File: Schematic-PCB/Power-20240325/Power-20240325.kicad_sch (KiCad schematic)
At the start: 10 parts, among them J1 Conn_01x02_Pin, Q1 NMOS, Q2 PMOS, U1 PIC12F683-IMC

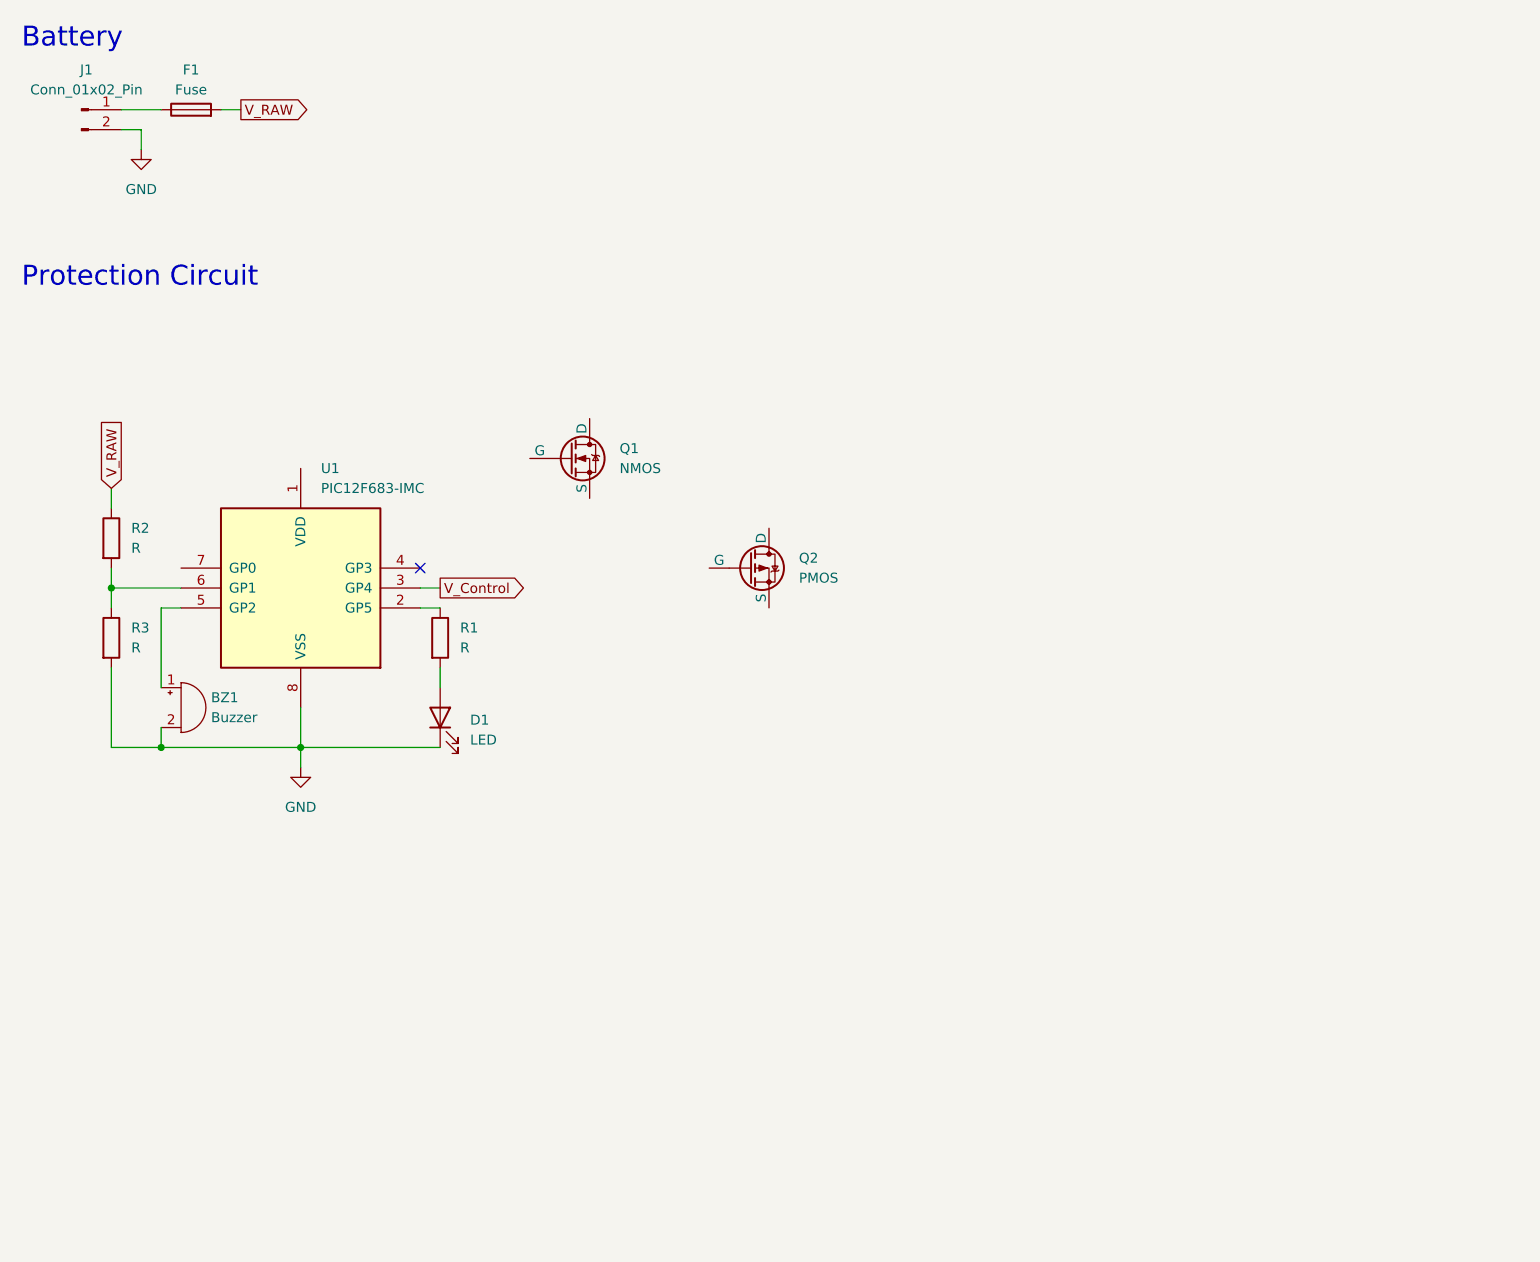
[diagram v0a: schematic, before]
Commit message: 電源基板の回路図を編集した
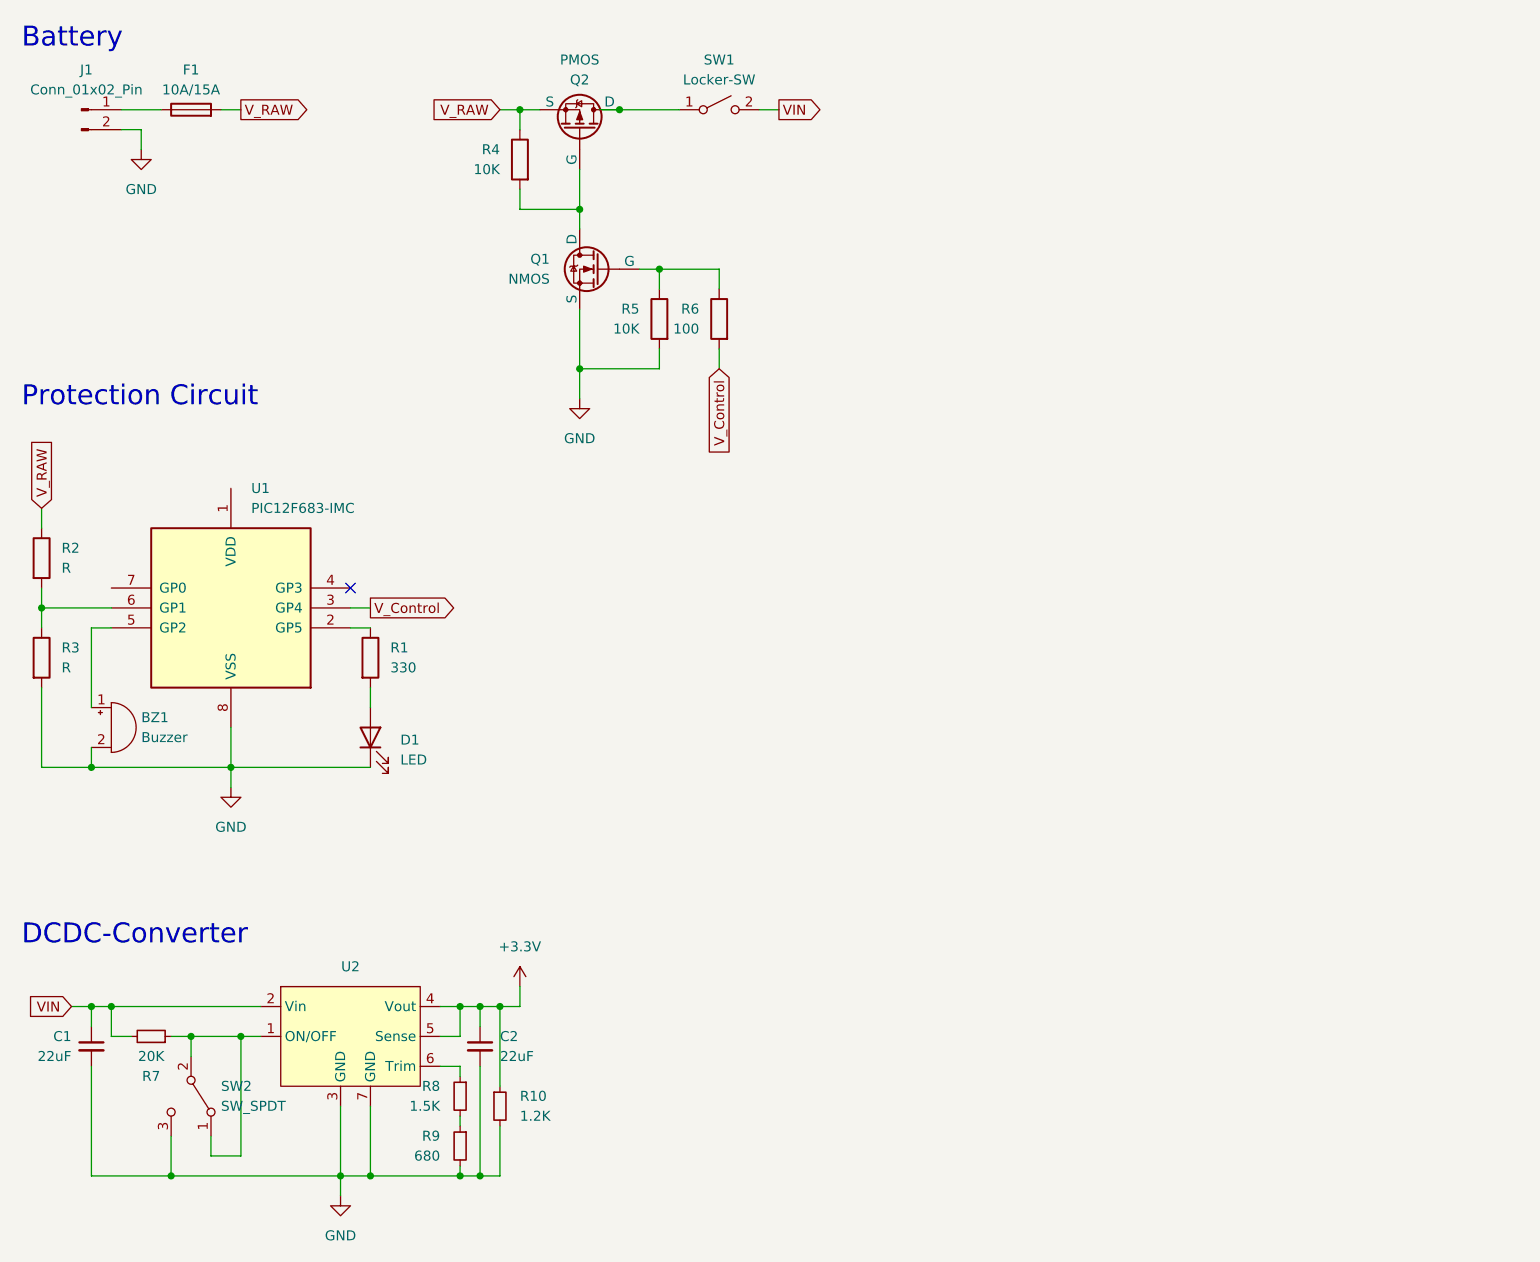
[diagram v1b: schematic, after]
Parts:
- added C1, C2: 22uF, symbol Device:C_Small
- added R10: 1.2K, symbol Device:R_Small
- added R4, R5: 10K, symbol Device:R
- added R6: 100, symbol Device:R
- added R7: 20K, symbol Device:R_Small
- added R8: 1.5K, symbol Device:R_Small
- added R9: 680, symbol Device:R_Small
- added SW1: Locker-SW, symbol Switch:SW_SPST
- added SW2: SW_SPDT, symbol Switch:SW_SPDT
- added U2: ~, @2024-Power:OKL-T6-W12N-C, symbol @2024-Power:OKL-T/6-W12
- F1: value Fuse -> 10A/15A
- R1: value R -> 330
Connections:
- net GND: now also Q1.3 (S), C1.2, C2.2, R10.2, R5.2, R9.2, SW2.3 (C), U2.3 (GND), U2.7 (GND)
- net V_Control: now also R6.2
- net V_RAW: now also Q2.3 (S), R4.1
- net at Q2.1 (D): now also SW1.1 (A)
- net at Q2.2 (G): now also Q1.2 (D), R4.2
- net at Q1.1 (G): now also R5.1, R6.1
- new net: R8.2, R9.1
- new net: R8.1, U2.6 (Trim)
- new net: R7.1, SW2.1 (A), SW2.2 (B), U2.1 (ON/OFF)
- new net +3.3V: C2.1, R10.1, U2.4 (Vout), U2.5 (Sense)
- new net VIN: C1.1, R7.2, SW1.2 (B), U2.2 (Vin)
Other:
- note added: "DCDC-Converter"
- moved on the sheet: BZ1, D1, Q1, Q2, R1, R2, R3, U1

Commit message: キッカー・MD・ラインセンサ・電源基板を更新
キッカー :
・基板外形変更後のPCBの修正が途中で止まっていたため、残りの部分を編集した

ラインセンサ :
・以前のラインセンサ回路を、コンパレータを使用する回路へと置換した
・ラベル line_threshold を、PWM出力可能な5番ピンに設定した

MD :
・キッカーもMD基板を経由させるように変更した
・ラインセンサ用にレベル変換回路を作成した

電源基板 :
・フットプリントを一部指定した
・基板外形をインポートした
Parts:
- C1, C2: footprint (none) -> Capacitor_SMD:C_0603_1608Metric
- D1: footprint (none) -> LED_SMD:LED_0805_2012Metric
- Q1: footprint (none) -> Package_TO_SOT_SMD:SOT-23
- Q2: footprint (none) -> Package_TO_SOT_SMD:TO-252-2
- R1, R10, R4, R5, R6, R7, R8, R9: footprint (none) -> Resistor_SMD:R_0603_1608Metric

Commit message: 電源基板を更新しました
回路図のDRをお願いします。
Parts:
- added C3, C4: 22uF, Capacitor_SMD:C_0603_1608Metric, symbol Device:C_Small
- added C5: 2.2uF, symbol Device:C_Small
- added C6: 1.0uF, symbol Device:C_Small
- added C7, C8: 1000uF, symbol Device:C
- added J2: Conn_01x05_Pin, symbol Connector:Conn_01x05_Pin
- added J3, J4, J5, J6: Conn_01x02_Pin, symbol Connector:Conn_01x02_Pin
- added R11: 20K, Resistor_SMD:R_0603_1608Metric, symbol Device:R_Small
- added R12: 1K, symbol Device:R_Small
- added R13: 330, Resistor_SMD:R_0603_1608Metric, symbol Device:R_Small
- added R14: 1.2K, Resistor_SMD:R_0603_1608Metric, symbol Device:R_Small
- added R15: 10, symbol Device:R_Small
- added SW3: SW_SPDT, symbol Switch:SW_SPDT
- added U3: ~, @2024-Power:OKL-T6-W12N-C, symbol @2024-Power:OKL-T/6-W12
- added U4: ~, Package_TO_SOT_SMD:SOT-89-3, symbol @2024-Power:NJW4183U3
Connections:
- net +3.3V: now also J5.1 (Pin_1)
- net GND: now also C3.2, C4.2, C5.2, C6.2, C7.2, C8.2, J2.3 (Pin_3), J3.2 (Pin_2), J4.2 (Pin_2), J5.2 (Pin_2), J6.2 (Pin_2), R14.2, R15.1, SW3.3 (C), U3.3 (GND), U3.7 (GND), U4.2 (GND)
- net VIN: now also C3.1, C7.1, C8.1, J3.1 (Pin_1), J6.1 (Pin_1), R11.2, U3.2 (Vin)
- net V_RAW: now also C6.1, U4.3 (VIN)
- net ICSPCLK: now reaches R2.2, R3.1, U1.6 (GP1)
- net ICSPCLK: now also J2.5 (Pin_5)
- net +3.3VA: now reaches U1.1 (VDD)
- net +3.3VA: now also C5.1, J2.2 (Pin_2), U4.1 (VOUT)
- net MCLR/VPP: now reaches U1.4 (GP3)
- net MCLR/VPP: now also J2.1 (Pin_1)
- net ICSPDAT: now reaches U1.7 (GP0)
- net ICSPDAT: now also J2.4 (Pin_4)
- new net: R12.1, U3.6 (Trim)
- new net: R12.2, R13.1
- new net: R13.2, R15.2
- new net: R11.1, SW3.1 (A), SW3.2 (B), U3.1 (ON/OFF)
- new net +5V: C4.1, J4.1 (Pin_1), R14.1, U3.4 (Vout), U3.5 (Sense)
- no-connect marks 1 -> 0
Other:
- note added: "Battery-IN"
- note added: "Kicker"
- note added: "Line"
- note added: "MD"
- note added: "Main"
- note added: "PIC Prog.IN"
- note removed: "Battery"
- moved on the sheet: BZ1, D1, Q1, Q2, R1, R2, R3, R4, R5, R6, SW1, U1

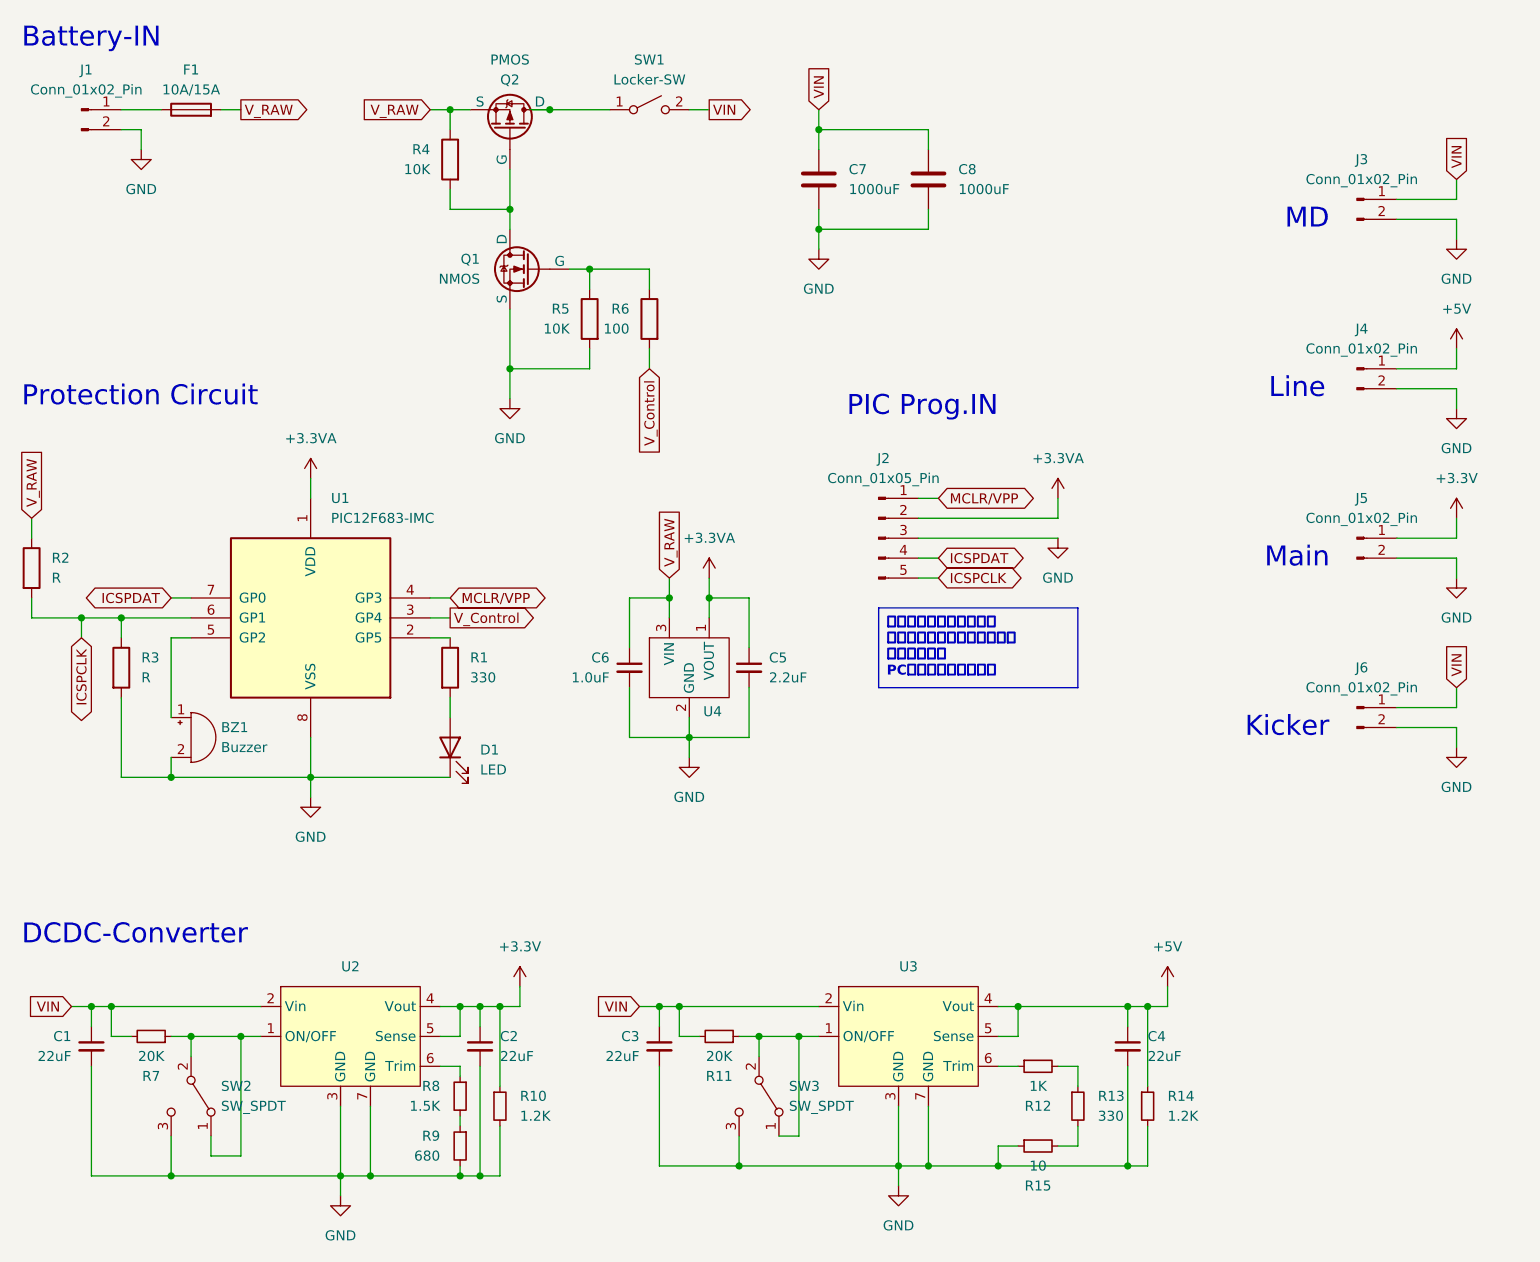
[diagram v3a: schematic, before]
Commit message: 電源基板PCBの途中まで
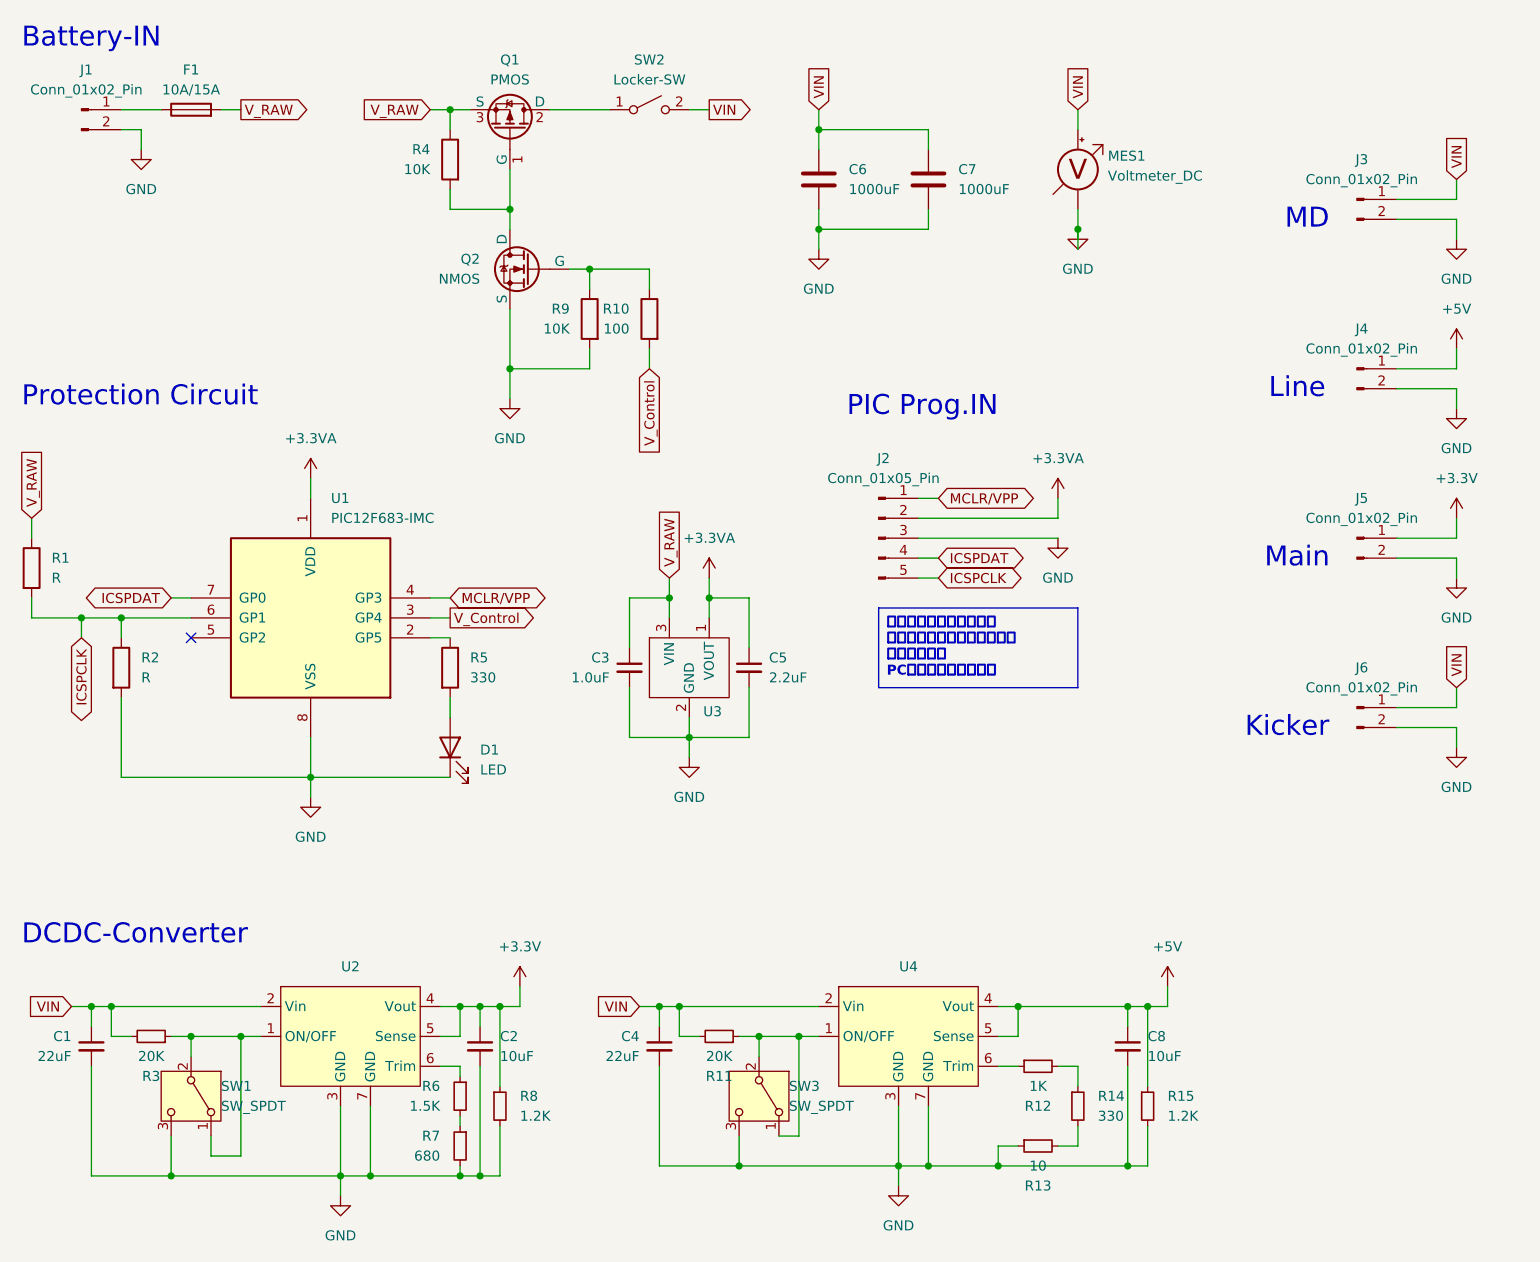
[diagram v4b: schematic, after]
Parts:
- removed BZ1: Buzzer, symbol Device:Buzzer
- removed Q2: PMOS, Package_TO_SOT_SMD:TO-252-2, symbol Simulation_SPICE:PMOS
- added MES1: Voltmeter_DC, @2024-Power:VoltMeter, symbol Device:Voltmeter_DC
- added Q1: PMOS, Package_TO_SOT_SMD:TO-252-2, symbol Simulation_SPICE:PMOS
- C2: value 22uF -> 10uF
- C3: renamed from C6; footprint (none) -> Capacitor_SMD:C_0603_1608Metric
- C5: footprint (none) -> Capacitor_SMD:C_0603_1608Metric
- C6: renamed from C7; footprint (none) -> Capacitor_THT:CP_Radial_D10.0mm_P5.00mm
- C7: renamed from C8; footprint (none) -> Capacitor_THT:CP_Radial_D10.0mm_P5.00mm
- C8: renamed from C4; value 22uF -> 10uF
- F1: footprint (none) -> @2024-Power:Fuse
- J1: footprint (none) -> Connector_JST:JST_VH_B2P-VH-B_1x02_P3.96mm_Vertical
- J2: footprint (none) -> Connector_PinSocket_2.54mm:PinSocket_1x05_P2.54mm_Vertical
- J4: footprint (none) -> Connector_JST:JST_VH_S2P-VH_1x02_P3.96mm_Horizontal
- J5, J6: footprint (none) -> Connector_JST:JST_XH_B2B-XH-A_1x02_P2.50mm_Vertical
- R1: renamed from R2; footprint (none) -> Resistor_THT:R_Axial_DIN0207_L6.3mm_D2.5mm_P7.62mm_Horizontal
- R12: footprint (none) -> Resistor_SMD:R_0603_1608Metric
- R13: renamed from R15; footprint (none) -> Resistor_SMD:R_0603_1608Metric
- R2: renamed from R3; footprint (none) -> Resistor_THT:R_Axial_DIN0207_L6.3mm_D2.5mm_P7.62mm_Horizontal
- SW1: renamed from SW2; footprint (none) -> @2024-Power:SS12D01G4
- SW2: renamed from SW1; footprint (none) -> @2024-Power:RA1113112R
- SW3: footprint (none) -> @2024-Power:SS12D01G4
- U1: footprint Package_DIP:DIP-8_W7.62mm -> Package_SO:SOP-8_3.76x4.96mm_P1.27mm
- renumbered C3 to C4, Q1 to Q2, R6 to R10, R13 to R14, R14 to R15, R7 to R3, R1 to R5, R8 to R6, R9 to R7, R10 to R8, R5 to R9, U4 to U3, U3 to U4
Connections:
- net GND: now also MES1.1 (-)
- net VIN: now also MES1.2 (+)
- net V_RAW: now also Q1.3 (S)
- net at Q2.2 (D), R4.2: now also Q1.1 (G)
- net at SW2.1 (A): now also Q1.2 (D)
- no-connect marks 0 -> 1
